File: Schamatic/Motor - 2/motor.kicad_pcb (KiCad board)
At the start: 2 copper layers, 45 x 45 mm, 84 parts, among them J1 CONN_02X05, J11 V, J12 U, J13 W, J3 RS485, J6 +BAT, J9 GND, Q1 PSMN3R3-40YS, Q2 PSMN3R3-40YS, Q3 PSMN3R3-40YS, Q4 PSMN3R3-40YS, Q5 PSMN3R3-40YS, Q6 PSMN3R3-40YS, Q7 NTR5103N, SW1 B3U-1000P, SW2 B3U-1000P, U1 MAX17502, U2 LTC2876, U3 MA700, U4 LM5019, U5 STM32F031G6U6, U6 AUIRS20302, Y1 8MhZ

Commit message: progress
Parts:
- removed C12: 3300pF, Capacitors_SMD:C_0603
- removed C13: 22uF, Capacitors_SMD:C_0805
- removed C8: 0.1uF, Capacitors_SMD:C_0603
- removed L1: 15uH, Inductors_SMD:L_1210
- removed the REF** at (82.0, 46.4)
- removed the REF** at (70.5, 50.2)
- removed the REF** at (59.9, 44.2)
- removed the REF** at (77.8, 53.6)
- removed the REF** at (87.0, 74.5)
- removed the REF** at (85.8, 75.8)
- removed the REF** at (84.2, 74.8)
- removed the REF** at (84.7, 76.3)
- removed the REF** at (64.3, 51.1)
- removed the REF** at (66.0, 50.2)
- removed the REF** at (64.0, 49.6)
- removed the REF** at (78.2, 46.8)
- removed the REF** at (65.8, 52.5)
- removed the REF** at (74.2, 53.0)
- removed the REF** at (78.8, 44.8)
- removed the REF** at (85.7, 50.9)
- removed the REF** at (69.8, 44.4)
- removed the REF** at (73.8, 49.9)
- removed the REF** at (77.7, 52.9)
- removed the REF** at (83.4, 59.1)
- added C2: 0.1uF, Capacitors_SMD:C_0603, F.Cu at (70.5, 72.8)
- added REF**: VIA-0.4, Dizzy:VIA-0.4, F.Cu at (71.9, 70.5)
- added REF**: VIA-0.4, Dizzy:VIA-0.4, F.Cu at (71.9, 69.5)
- added REF**: VIA-0.4, Dizzy:VIA-0.4, F.Cu at (69.7, 73.5)
- added REF**: VIA-0.4, Dizzy:VIA-0.4, F.Cu at (73.4, 74.5)
- added REF**: VIA-0.4, Dizzy:VIA-0.4, F.Cu at (77.3, 74.0)
- added REF**: VIA-0.4, Dizzy:VIA-0.4, F.Cu at (76.7, 74.8)
- added REF**: VIA-0.4, Dizzy:VIA-0.4, F.Cu at (86.2, 77.5)
- added REF**: VIA-0.4, Dizzy:VIA-0.4, F.Cu at (84.3, 75.0)
- added REF**: VIA-0.4, Dizzy:VIA-0.4, F.Cu at (86.3, 75.2)
- added REF**: VIA-0.4, Dizzy:VIA-0.4, F.Cu at (74.0, 51.5)
- added REF**: VIA-0.4, Dizzy:VIA-0.4, F.Cu at (73.3, 51.5)
- added REF**: VIA-0.4, Dizzy:VIA-0.4, F.Cu at (75.9, 51.8)
- added REF**: VIA-0.4, Dizzy:VIA-0.4, F.Cu at (75.9, 54.4)
- added REF**: VIA-0.4, Dizzy:VIA-0.4, F.Cu at (74.7, 54.6)
- added REF**: VIA-0.4, Dizzy:VIA-0.4, F.Cu at (70.8, 59.4)
- added REF**: VIA-0.4, Dizzy:VIA-0.4, F.Cu at (70.2, 54.9)
- added REF**: VIA-0.4, Dizzy:VIA-0.4, F.Cu at (69.5, 55.0)
- added REF**: VIA-0.4, Dizzy:VIA-0.4, F.Cu at (64.0, 49.8)
- added REF**: VIA-0.4, Dizzy:VIA-0.4, F.Cu at (65.7, 50.5)
- added REF**: VIA-0.4, Dizzy:VIA-0.4, F.Cu at (68.0, 51.5)
- added REF**: VIA-0.4, Dizzy:VIA-0.4, F.Cu at (70.5, 51.9)
- added REF**: VIA-0.4, Dizzy:VIA-0.4, F.Cu at (86.3, 53.1)
- added REF**: VIA-0.4, Dizzy:VIA-0.4, F.Cu at (78.7, 44.8)
- added REF**: VIA-0.4, Dizzy:VIA-0.4, F.Cu at (77.7, 81.8)
- added REF**: VIA-0.4, Dizzy:VIA-0.4, F.Cu at (71.3, 81.2)
- added REF**: VIA-0.4, Dizzy:VIA-0.4, F.Cu at (70.9, 75.8)
- added REF**: VIA-0.4, Dizzy:VIA-0.4, F.Cu at (69.2, 75.7)
- added REF**: VIA-0.4, Dizzy:VIA-0.4, F.Cu at (65.9, 73.9)
- added REF**: VIA-0.4, Dizzy:VIA-0.4, F.Cu at (73.7, 73.7)
- C1: value 1uF -> 0.1uF
- Q7: footprint TO_SOT_Packages_SMD:SOT-23 -> TO_SOT_Packages_SMD:SOT-323_SC-70
- R12: value 230K -> 30k 1%
- R13: value 10K -> 10K 1%
- R15: value 390 -> 600
- U1: value MAX17502 -> TPS73433DRV; footprint Housings_DFN_QFN:DFN-10-1EP_2x3mm_Pitch0.5mm -> Housings_DFN_QFN:DFN-6-1EP_2x2mm_Pitch0.65mm
- U3: value MA700 -> A1335; footprint Housings_DFN_QFN:QFN-16-1EP_3x3mm_Pitch0.5mm -> Housings_SSOP:TSSOP-14_4.4x5mm_Pitch0.65mm
- U5: value STM32F031G6U6 -> STM32F031K6U6
- moved C1 15.5 mm to (70.5, 70.0), turned to 90 degrees
- moved U1 3.29 mm to (73.7, 51.5), turned to 90 degrees
- moved R14 1.03 mm to (73.1, 45.1)
- moved U3 0.55 mm to (65.5, 71.5), turned to 180 degrees
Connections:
- C1 pad 1: Net-(C1-Pad1) -> +5V
- C11 pad 1: Net-(C11-Pad1) -> +5V
- C3 pad 1: Net-(C3-Pad1) -> DRV
- D4 pad 1: Net-(C3-Pad1) -> DRV
- D7 pad 2: +3V3 -> Net-(D7-Pad2)
- L2 pad 2: +24V -> Net-(D7-Pad2)
- Q7 pad 3: +24V -> DRV
- R10 pad 2: Net-(C3-Pad1) -> DRV
- R12 pad 1: +24V -> Net-(D7-Pad2)
- R14 pad 1: +24V -> Net-(D7-Pad2)
- R14 pad 2: Net-(C11-Pad1) -> +5V
- R9 pad 1: +24V -> DRV
- U1 pad 1: Earth -> +3V3
- U1 pad 2: +24V -> (no net)
- U1 pad 3: +24V -> Earth
- U1 pad 4: Net-(C1-Pad1) -> Net-(D7-Pad2)
- U1 pad 5: +3V3 -> (no net)
- U1 pad 6: Net-(C12-Pad2) -> Net-(D7-Pad2)
- U1 pad 7: (no net) -> Earth
- U3 pad 1: (no net) -> Earth
- U3 pad 10: (no net) -> MISO
- U3 pad 11: (no net) -> SCK
- U3 pad 12: SCK -> MOSI
- U3 pad 13: +3V3 -> CS
- U3 pad 14: (no net) -> Earth
- U3 pad 2: (no net) -> Net-(C2-Pad1)
- U3 pad 3: (no net) -> Earth
- U3 pad 4: MOSI -> (no net)
- U3 pad 5: CS -> +5V
- U3 pad 7: MISO -> Earth
- U3 pad 8: Earth -> Net-(C2-Pad1)
- U4 pad 2: Net-(C3-Pad1) -> DRV
- U4 pad 3: Net-(C3-Pad1) -> DRV
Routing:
- net DRV: track 0.00 -> 58.8 mm, vias 0 -> 2
- net +5V: track 0.00 -> 53.5 mm
- net +24V: track 47.6 -> 0.00 mm, vias 7 -> 0
- net +3V3: track 117.3 -> 87.2 mm, vias 7 -> 4
- net Net-(D7-Pad2): track 0.00 -> 17.0 mm
- net Earth: track 60.8 -> 48.8 mm, vias 14 -> 12
- net Net-(C3-Pad1): track 9.67 -> 0.00 mm
- net Net-(C2-Pad1): track 0.00 -> 9.58 mm
- net SCK: track 12.4 -> 18.0 mm
- net Net-(C12-Pad2): track 5.46 -> 0.00 mm, vias 2 -> 0
- net Net-(C11-Pad1): track 3.30 -> 0.00 mm
- net Net-(C1-Pad1): track 2.69 -> 0.00 mm
- net CS: track 15.7 -> 17.8 mm, vias 0 -> 2
- net Net-(SW1-Pad2): track 22.4 -> 20.9 mm
- net Net-(L1-Pad1): track 1.56 -> 0.00 mm
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- removed copper zone on F.Cu, net +24V

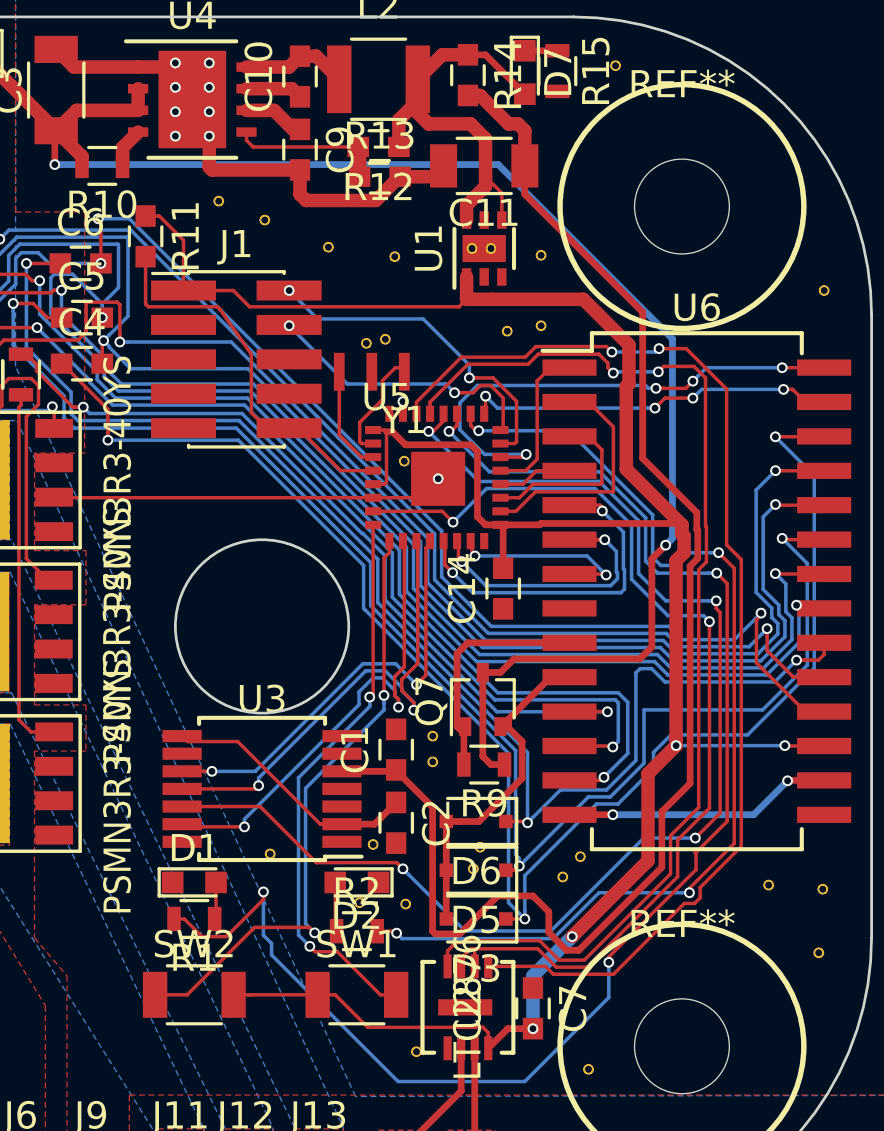
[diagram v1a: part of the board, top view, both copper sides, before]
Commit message: 3.3V MA700
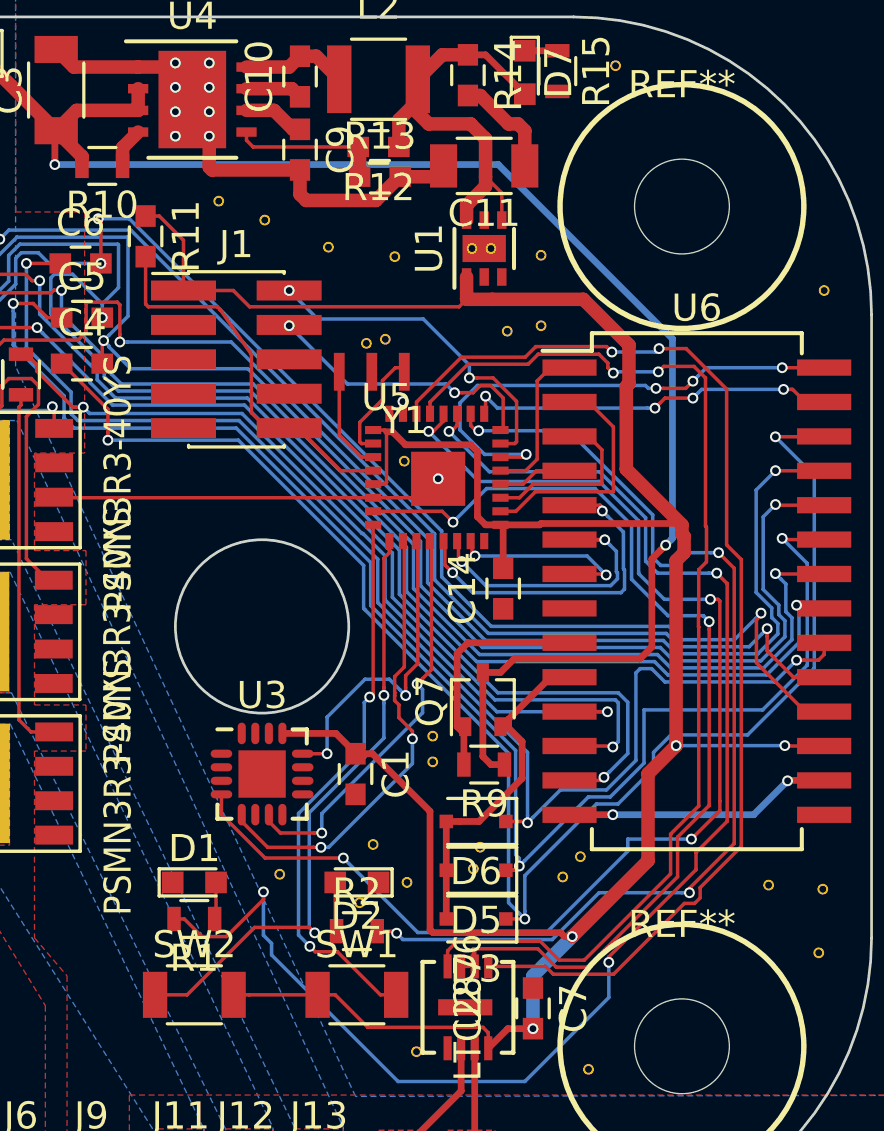
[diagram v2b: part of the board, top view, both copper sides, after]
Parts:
- removed C2: 0.1uF, Capacitors_SMD:C_0603
- U3: value A1335 -> MA700; footprint Housings_SSOP:TSSOP-14_4.4x5mm_Pitch0.65mm -> Housings_DFN_QFN:UQFN-16-1EP_3x3mm_Pitch0.5mm
- moved C1 1.75 mm to (69.0, 71.0), turned to 270 degrees
- moved REF** 0.83 mm to (66.2, 74.7)
- moved REF** 0.80 mm to (71.0, 75.0)
- moved U3 0.55 mm to (65.5, 71.0), turned to 0 degrees
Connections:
- C1 pad 1: +5V -> +3V3
- C11 pad 1: +5V -> Net-(C11-Pad1)
- R14 pad 2: +5V -> Net-(C11-Pad1)
- U3 pad 1: Earth -> (no net)
- U3 pad 10: MISO -> (no net)
- U3 pad 11: SCK -> (no net)
- U3 pad 12: MOSI -> SCK
- U3 pad 13: CS -> +3V3
- U3 pad 14: Earth -> (no net)
- U3 pad 2: Net-(C2-Pad1) -> (no net)
- U3 pad 3: Earth -> (no net)
- U3 pad 4: (no net) -> MOSI
- U3 pad 5: +5V -> CS
- U3 pad 7: Earth -> MISO
- U3 pad 8: Net-(C2-Pad1) -> Earth
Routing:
- net +5V: track 53.5 -> 0.00 mm
- net +3V3: track 87.2 -> 103.6 mm
- net Net-(C2-Pad1): track 9.58 -> 0.00 mm
- net SCK: track 18.0 -> 11.8 mm
- net Net-(C11-Pad1): track 0.00 -> 4.29 mm
- net MISO: track 16.1 -> 14.9 mm
- net CS: track 17.8 -> 16.8 mm
- net MOSI: track 46.8 -> 46.3 mm

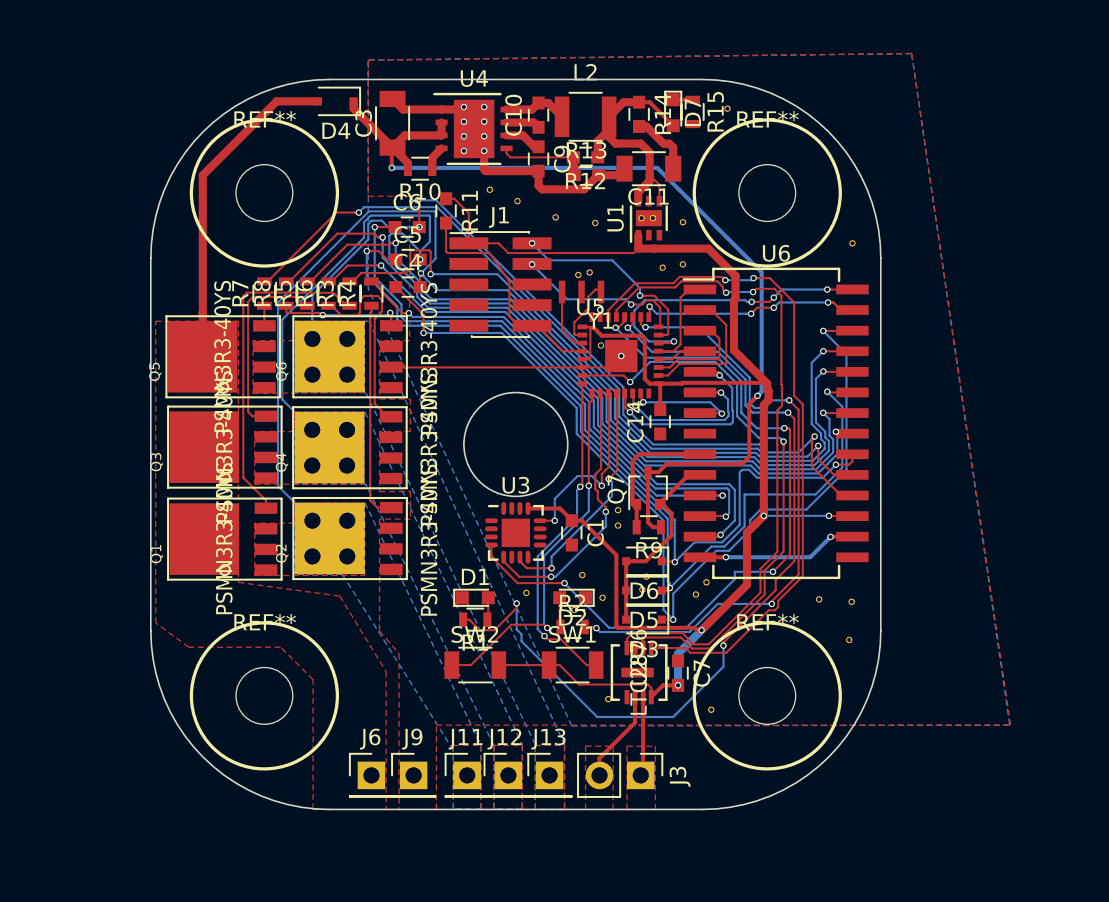
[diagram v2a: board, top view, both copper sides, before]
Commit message: new drivers
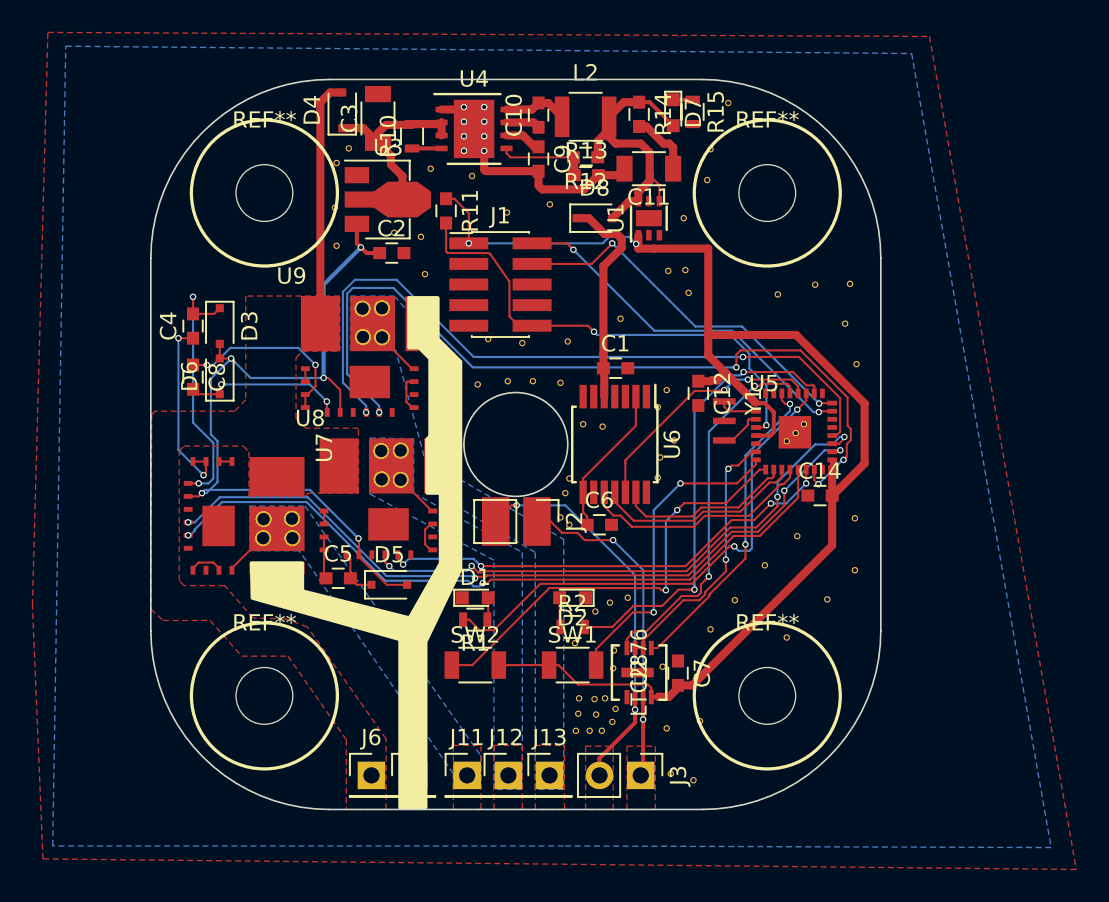
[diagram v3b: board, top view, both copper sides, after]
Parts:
- removed Q1, Q3, Q5: PSMN3R3-40YS, Dizzy:PSMN3R3-40YS
- removed Q2, Q4, Q6: PSMN3R3-40YS, Dizzy:PSMN3R3-40YS-vias
- removed Q7: NTR5103N, TO_SOT_Packages_SMD:SOT-323_SC-70
- removed R3, R4, R5, R6, R7, R8: 10, Resistors_SMD:R_0603
- removed R9: 100K, Resistors_SMD:R_0603
- removed the REF** at (71.9, 70.5)
- removed the REF** at (71.9, 69.5)
- removed the REF** at (69.7, 73.5)
- removed the REF** at (73.4, 74.5)
- removed the REF** at (77.3, 74.0)
- removed the REF** at (76.7, 74.8)
- removed the REF** at (86.2, 77.5)
- removed the REF** at (84.3, 75.0)
- removed the REF** at (86.3, 75.2)
- removed the REF** at (74.0, 51.5)
- removed the REF** at (73.3, 51.5)
- removed the REF** at (75.9, 51.8)
- removed the REF** at (75.9, 54.4)
- removed the REF** at (74.7, 54.6)
- removed the REF** at (70.8, 59.4)
- removed the REF** at (70.2, 54.9)
- removed the REF** at (69.5, 55.0)
- removed the REF** at (64.0, 49.8)
- removed the REF** at (65.7, 50.5)
- removed the REF** at (68.0, 51.5)
- removed the REF** at (70.5, 51.9)
- removed the REF** at (86.3, 53.1)
- removed the REF** at (78.7, 44.8)
- removed the REF** at (77.7, 81.8)
- removed the REF** at (71.3, 81.2)
- removed the REF** at (71.0, 75.0)
- removed the REF** at (69.2, 75.7)
- removed the REF** at (66.2, 74.7)
- removed the REF** at (73.7, 73.7)
- added C12: 0.1uF, Capacitors_SMD:C_0603, F.Cu at (76.8, 62.4)
- added C2: 1uF, Capacitors_SMD:C_0603, F.Cu at (57.9, 53.7)
- added C8: 1uF, Capacitors_SMD:C_0603, F.Cu at (45.6, 61.4)
- added D8: D_Small, Diodes_SMD:D_SOD-323F, F.Cu at (70.3, 51.5)
- added J2: RS485, Pin_Headers:Pin_Header_Straight_1x02_Pitch2.54mm, F.Cu at (66.8, 70.2)
- added REF**: VIA-0.4, Dizzy:VIA-0.4, F.Cu at (68.9, 67.6)
- added REF**: VIA-0.4, Dizzy:VIA-0.4, F.Cu at (71.1, 81.2)
- added REF**: VIA-0.4, Dizzy:VIA-0.4, F.Cu at (70.5, 81.2)
- added REF**: VIA-0.4, Dizzy:VIA-0.4, F.Cu at (69.5, 81.2)
- added REF**: VIA-0.4, Dizzy:VIA-0.4, F.Cu at (83.3, 64.2)
- added REF**: VIA-0.4, Dizzy:VIA-0.4, F.Cu at (82.8, 64.8)
- added REF**: VIA-0.4, Dizzy:VIA-0.4, F.Cu at (82.3, 65.3)
- added REF**: VIA-0.4, Dizzy:VIA-0.4, F.Cu at (74.3, 67.5)
- added REF**: VIA-0.4, Dizzy:VIA-0.4, F.Cu at (74.5, 66.3)
- added REF**: VIA-0.4, Dizzy:VIA-0.4, F.Cu at (75.3, 65.2)
- added REF**: VIA-0.4, Dizzy:VIA-0.4, F.Cu at (74.3, 63.2)
- added REF**: VIA-0.4, Dizzy:VIA-0.4, F.Cu at (68.9, 70.5)
- added REF**: VIA-0.4, Dizzy:VIA-0.4, F.Cu at (74.9, 62.1)
- added REF**: VIA-0.4, Dizzy:VIA-0.4, F.Cu at (78.7, 44.5)
- added REF**: VIA-0.4, Dizzy:VIA-0.4, F.Cu at (77.6, 47.3)
- added REF**: VIA-0.4, Dizzy:VIA-0.4, F.Cu at (77.4, 49.2)
- added REF**: VIA-0.4, Dizzy:VIA-0.4, F.Cu at (76.0, 51.5)
- added REF**: VIA-0.4, Dizzy:VIA-0.4, F.Cu at (67.7, 50.7)
- added REF**: VIA-0.4, Dizzy:VIA-0.4, F.Cu at (65.0, 51.2)
- added REF**: VIA-0.4, Dizzy:VIA-0.4, F.Cu at (62.9, 49.0)
- added REF**: VIA-0.4, Dizzy:VIA-0.4, F.Cu at (60.4, 48.5)
- added REF**: VIA-0.4, Dizzy:VIA-0.4, F.Cu at (55.3, 47.2)
- added REF**: VIA-0.4, Dizzy:VIA-0.4, F.Cu at (70.5, 82.2)
- added REF**: VIA-0.4, Dizzy:VIA-0.4, F.Cu at (54.5, 48.1)
- added REF**: VIA-0.4, Dizzy:VIA-0.4, F.Cu at (54.5, 50.9)
- added REF**: VIA-0.4, Dizzy:VIA-0.4, F.Cu at (54.5, 53.2)
- added REF**: VIA-0.4, Dizzy:VIA-0.4, F.Cu at (58.1, 52.5)
- added REF**: VIA-0.4, Dizzy:VIA-0.4, F.Cu at (59.8, 52.7)
- added REF**: VIA-0.4, Dizzy:VIA-0.4, F.Cu at (60.0, 55.0)
- added REF**: VIA-0.4, Dizzy:VIA-0.4, F.Cu at (76.5, 86.2)
- added REF**: VIA-0.4, Dizzy:VIA-0.4, F.Cu at (75.2, 85.8)
- added REF**: VIA-0.4, Dizzy:VIA-0.4, F.Cu at (74.9, 83.0)
- added REF**: VIA-0.4, Dizzy:VIA-0.4, F.Cu at (77.0, 82.5)
- added REF**: VIA-0.4, Dizzy:VIA-0.4, F.Cu at (69.5, 82.1)
- added REF**: VIA-0.4, Dizzy:VIA-0.4, F.Cu at (82.3, 77.4)
- added REF**: VIA-0.4, Dizzy:VIA-0.4, F.Cu at (84.8, 75.0)
- added REF**: VIA-0.4, Dizzy:VIA-0.4, F.Cu at (86.5, 73.2)
- added REF**: VIA-0.4, Dizzy:VIA-0.4, F.Cu at (86.5, 70.0)
- added REF**: VIA-0.4, Dizzy:VIA-0.4, F.Cu at (83.0, 71.2)
- added REF**: VIA-0.4, Dizzy:VIA-0.4, F.Cu at (81.0, 73.0)
- added REF**: VIA-0.4, Dizzy:VIA-0.4, F.Cu at (79.1, 75.1)
- added REF**: VIA-0.4, Dizzy:VIA-0.4, F.Cu at (77.6, 76.9)
- added REF**: VIA-0.4, Dizzy:VIA-0.4, F.Cu at (74.7, 79.2)
- added REF**: VIA-0.4, Dizzy:VIA-0.4, F.Cu at (71.6, 79.3)
- added REF**: VIA-0.4, Dizzy:VIA-0.4, F.Cu at (69.3, 83.2)
- added REF**: VIA-0.4, Dizzy:VIA-0.4, F.Cu at (71.7, 78.2)
- added REF**: VIA-0.4, Dizzy:VIA-0.4, F.Cu at (69.2, 77.8)
- added REF**: VIA-0.4, Dizzy:VIA-0.4, F.Cu at (70.5, 75.8)
- added REF**: VIA-0.4, Dizzy:VIA-0.4, F.Cu at (72.5, 75.0)
- added REF**: VIA-0.4, Dizzy:VIA-0.4, F.Cu at (71.4, 75.2)
- added REF**: VIA-0.4, Dizzy:VIA-0.4, F.Cu at (68.3, 70.0)
- added REF**: VIA-0.4, Dizzy:VIA-0.4, F.Cu at (68.7, 68.5)
- added REF**: VIA-0.4, Dizzy:VIA-0.4, F.Cu at (71.0, 64.4)
- added REF**: VIA-0.4, Dizzy:VIA-0.4, F.Cu at (69.8, 64.2)
- added REF**: VIA-0.4, Dizzy:VIA-0.4, F.Cu at (68.3, 61.7)
- added REF**: VIA-0.4, Dizzy:VIA-0.4, F.Cu at (70.2, 83.2)
- added REF**: VIA-0.4, Dizzy:VIA-0.4, F.Cu at (66.7, 61.6)
- added REF**: VIA-0.4, Dizzy:VIA-0.4, F.Cu at (65.1, 61.6)
- added REF**: VIA-0.4, Dizzy:VIA-0.4, F.Cu at (63.2, 61.8)
- added REF**: VIA-0.4, Dizzy:VIA-0.4, F.Cu at (63.9, 59.0)
- added REF**: VIA-0.4, Dizzy:VIA-0.4, F.Cu at (66.0, 59.2)
- added REF**: VIA-0.4, Dizzy:VIA-0.4, F.Cu at (68.8, 59.1)
- added REF**: VIA-0.4, Dizzy:VIA-0.4, F.Cu at (72.0, 57.8)
- added REF**: VIA-0.4, Dizzy:VIA-0.4, F.Cu at (86.6, 60.5)
- added REF**: VIA-0.4, Dizzy:VIA-0.4, F.Cu at (76.2, 56.1)
- added REF**: VIA-0.4, Dizzy:VIA-0.4, F.Cu at (76.0, 54.8)
- added REF**: VIA-0.4, Dizzy:VIA-0.4, F.Cu at (70.9, 83.2)
- added REF**: VIA-0.4, Dizzy:VIA-0.4, F.Cu at (75.0, 54.8)
- added REF**: VIA-0.4, Dizzy:VIA-0.4, F.Cu at (86.2, 55.6)
- added REF**: VIA-0.4, Dizzy:VIA-0.4, F.Cu at (85.9, 58.0)
- added REF**: VIA-0.4, Dizzy:VIA-0.4, F.Cu at (84.0, 55.6)
- added REF**: VIA-0.4, Dizzy:VIA-0.4, F.Cu at (81.8, 56.2)
- added REF**: VIA-0.4, Dizzy:VIA-0.4, F.Cu at (71.5, 82.6)
- added REF**: VIA-0.4, Dizzy:VIA-0.4, F.Cu at (71.8, 81.8)
- added U7: IRSM005, Dizzy:IRSM005, F.Cu at (54.2, 65.7)
- added U8: IRSM005, Dizzy:IRSM005, F.Cu at (52.8, 63.4)
- added U9: IRSM005, Dizzy:IRSM005, F.Cu at (51.7, 54.6)
- C6: value 1uF -> 0.1uF
- U3: value MA700 -> ZXTR2012Z; footprint Housings_DFN_QFN:UQFN-16-1EP_3x3mm_Pitch0.5mm -> TO_SOT_Packages_SMD:SOT-89-3
- U6: value AUIRS20302 -> A1335; footprint Housings_SOIC:SOIC-28W_7.5x18.7mm_Pitch1.27mm -> Housings_SSOP:TSSOP-14_4.4x5mm_Pitch0.65mm
- moved D3 31.8 mm to (47.2, 58.2), turned to 270 degrees
- moved D6 28.5 mm to (47.2, 61.3), turned to 90 degrees
- moved U3 22.2 mm to (57.2, 50.4)
- moved C6 21.8 mm to (70.7, 70.5)
- moved C5 20.1 mm to (54.5, 73.8)
- moved D5 15.7 mm to (57.7, 74.2), turned to 0 degrees
- moved C4 13.5 mm to (45.6, 58.2), turned to 90 degrees
- moved U5 11.7 mm to (80.3, 63.0)
- moved Y1 10.9 mm to (80.7, 62.9), turned to 270 degrees
- moved C14 10.9 mm to (84.2, 68.7), turned to 0 degrees
- moved C1 10.5 mm to (71.7, 60.8), turned to 0 degrees
- moved U6 10.0 mm to (71.6, 65.5), turned to 270 degrees
- moved R10 2.06 mm to (59.1, 46.5), turned to 90 degrees
- moved C3 0.95 mm to (57.0, 45.4)
- moved D4 0.68 mm to (54.8, 44.9), turned to 90 degrees
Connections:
- C1 pad 1: +3V3 -> 5V
- C3 pad 1: DRV -> Net-(C3-Pad1)
- C4 pad 1: BOOT1 -> Net-(C4-Pad1)
- C4 pad 2: O1 -> Net-(C4-Pad2)
- C5 pad 1: BOOT2 -> Net-(C5-Pad1)
- C5 pad 2: O2 -> Net-(C5-Pad2)
- C6 pad 1: BOOT3 -> Net-(C6-Pad1)
- C6 pad 2: O3 -> Earth
- D3 pad 1: BOOT1 -> Net-(C4-Pad2)
- D3 pad 2: Net-(D3-Pad2) -> 12V
- D4 pad 1: DRV -> Net-(C3-Pad1)
- D5 pad 1: BOOT2 -> Net-(C5-Pad2)
- D5 pad 2: Net-(D3-Pad2) -> 12V
- D6 pad 1: BOOT3 -> Net-(C8-Pad2)
- D6 pad 2: Net-(D3-Pad2) -> 12V
- J11 pad 1: O1 -> Net-(J11-Pad1)
- J12 pad 1: O2 -> Net-(J12-Pad1)
- J13 pad 1: O3 -> Net-(J13-Pad1)
- R10 pad 2: DRV -> Net-(C3-Pad1)
- U3 pad 1: (no net) -> Earth
- U3 pad 2: (no net) -> Net-(C3-Pad1)
- U3 pad 3: (no net) -> 12V
- U4 pad 2: DRV -> Net-(C3-Pad1)
- U4 pad 3: DRV -> Net-(C3-Pad1)
- U5 pad 21: EN -> (no net)
- U5 pad 22: FRST -> (no net)
- U5 pad 25: FLT -> (no net)
- U6 pad 1: EN -> Earth
- U6 pad 10: Net-(D3-Pad2) -> MISO
- U6 pad 11: L1 -> SCK
- U6 pad 12: L2 -> MOSI
- U6 pad 13: L3 -> CS
- U6 pad 2: HIN1 -> Net-(C6-Pad1)
- U6 pad 3: HIN2 -> Earth
- U6 pad 4: HIN3 -> (no net)
- U6 pad 5: LIN1 -> 5V
- U6 pad 6: LIN2 -> (no net)
- U6 pad 7: LIN3 -> Earth
- U6 pad 8: Earth -> Net-(C6-Pad1)
- U6 pad 9: VCP -> (no net)
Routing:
- net O1: track 70.0 -> 0.00 mm, vias 2 -> 0
- net O2: track 63.8 -> 0.00 mm, vias 2 -> 0
- net DRV: track 58.8 -> 0.00 mm, vias 2 -> 0
- net BOOT1: track 57.9 -> 0.00 mm, vias 3 -> 0
- net BOOT2: track 57.1 -> 0.00 mm, vias 3 -> 0
- net O3: track 51.1 -> 0.00 mm, vias 3 -> 0
- net BOOT3: track 50.2 -> 0.00 mm, vias 3 -> 0
- net 12V: track 0.00 -> 48.7 mm, vias 0 -> 5
- net H3: track 47.0 -> 0.00 mm, vias 2 -> 0
- net H1: track 46.6 -> 0.00 mm, vias 2 -> 0
- net H2: track 45.8 -> 0.00 mm, vias 2 -> 0
- net LIN3: track 7.06 -> 50.6 mm, vias 2 -> 4
- net HIN3: track 2.66 -> 44.7 mm, vias 0 -> 2
- net L3: track 41.7 -> 0.00 mm, vias 2 -> 0
- net HIN1: track 9.46 -> 47.4 mm, vias 0 -> 4
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- added copper zone on B.Cu, net Net-(J11-Pad1)
- added copper zone on B.Cu, net Net-(J12-Pad1)
- added copper zone on B.Cu, net Net-(J13-Pad1)
- removed copper zone on B.Cu, net O1
- removed copper zone on B.Cu, net O2
- removed copper zone on B.Cu, net O3
